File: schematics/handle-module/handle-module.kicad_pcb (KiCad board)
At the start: 4 copper layers, 80 x 42 mm, 115 parts, among them J1 2*LiFePo4@18650@1800mAh, 6,4V, J3 JST XH B3B, J4 USBASP, Q1 IRLML5203, Q10 IRLML0030, Q2 IRLML5203, Q3 IRLML0030, Q4 IRLML0030, Q5 IRLML0030, Q6 IRLML0030, Q7 IRLML0030, Q8 IRLML0030, Q9 IRLML0030, SW1 KLS7-TS3601-5.0-180, SW2 KLS7-TS3601-5.0-180, U1 STX882@443MHz, U2 SRX882@443MHz, U3 AMS1117-5.0, U4 MCP1703T-3302E, U5 ATmega328-A, U6 BQ24780S, X1 HC-49U, 8MHz

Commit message: Second board
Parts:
- moved C27 1.50 mm to (156.2, 79.7), turned to 180 degrees
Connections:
- C27 pad 2: GNDPWR -> GNDA
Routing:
- net GNDA: track 87.9 -> 99.0 mm
- net GNDPWR: track 156.4 -> 147.9 mm
- net /VBAT_BEFORE_FUSE: track 35.0 -> 33.3 mm
- net /CHARGER_SUPPLY: track 47.6 -> 47.0 mm
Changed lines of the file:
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@@
     (property "ki_keywords" "R res resistor")
     (attr smd)
-    (fp_text reference "R14" (at 0 1.65) (layer "B.SilkS")
+    (fp_text reference "R14" (at 3.1875 -0.7) (layer "B.SilkS")
         (effects (font (size 1 1) (thickness 0.15)) (justify mirror))
     )
@@
   )
   (footprint "Capacitor_SMD:C_0603_1608Metric" (layer "B.Cu")
-    (at 157.7 79.7)
+    (at 156.2 79.7 180)
     (descr "Capacitor SMD 0603 (1608 Metric), square (rectangular) end terminal, IPC_7351 nominal, (Body size source: IPC-SM-782 page 76, https://www.pcb-3d.com/wordpress/wp-content/uploads/ipc-sm-782a_amendment_1_and_2.pdf), generated with kicad-footprint-generator")
     (tags "capacitor")
@@
     (property "ki_keywords" "cap capacitor")
     (attr smd)
-    (fp_text reference "C27" (at 0 1.43) (layer "B.SilkS")
+    (fp_text reference "C27" (at 0.1 -1.5) (layer "B.SilkS")
         (effects (font (size 1 1) (thickness 0.15)) (justify mirror))
     )
@@
     (fp_line (start 0.8 0.4) (end 0.8 -0.4)
       (stroke (width 0.1) (type solid)) (layer "B.Fab"))
-    (pad "1" smd roundrect (at -0.775 0) (size 0.9 0.95) (layers "B.Cu" "B.Paste" "B.Mask") (roundrect_rratio 0.25)
+    (pad "1" smd roundrect (at -0.775 0 180) (size 0.9 0.95) (layers "B.Cu" "B.Paste" "B.Mask") (roundrect_rratio 0.25)
       (net 19 "Net-(U6-VCC)") (pintype "passive"))
-    (pad "2" smd roundrect (at 0.775 0) (size 0.9 0.95) (layers "B.Cu" "B.Paste" "B.Mask") (roundrect_rratio 0.25)
-      (net 6 "GNDPWR") (pintype "passive"))
+    (pad "2" smd roundrect (at 0.775 0 180) (size 0.9 0.95) (layers "B.Cu" "B.Paste" "B.Mask") (roundrect_rratio 0.25)
+      (net 1 "GNDA") (pintype "passive"))
     (model "${KICAD6_3DMODEL_DIR}/Capacitor_SMD.3dshapes/C_0603_1608Metric.wrl"
       (offset (xyz 0 0 0))
@@
     (effects (font (size 1.5 1.5) (thickness 0.2)) (justify left top))
   )
-  (segment (start 164.9 71.3625) (end 164.9 71.1) (width 0.2) (layer "F.Cu") (net 1))
   (segment (start 114.25 58.5) (end 113.8 58.05) (width 0.5) (layer "F.Cu") (net 1))
   (segment (start 174.55 67.05) (end 174.55 70.9375) (width 0.5) (layer "F.Cu") (net 1))
@@
   (segment (start 172.8 62.075001) (end 163 52.275001) (width 1) (layer "In1.Cu") (net 1))
   (segment (start 133.5 88.75) (end 130.5 85.75) (width 0.5) (layer "B.Cu") (net 1))
+  (segment (start 151.452449 77.8) (end 144.9 77.8) (width 0.5) (layer "B.Cu") (net 1))
   (segment (start 150.6375 88.75) (end 133.5 88.75) (width 0.5) (layer "B.Cu") (net 1))
+  (segment (start 153.352449 79.7) (end 151.452449 77.8) (width 0.5) (layer "B.Cu") (net 1))
+  (segment (start 155.425 79.7) (end 153.352449 79.7) (width 0.5) (layer "B.Cu") (net 1))
   (segment (start 151.6875 87.7) (end 150.6375 88.75) (width 0.5) (layer "B.Cu") (net 1))
   (segment (start 163.560051 78.2) (end 160.860051 80.9) (width 0.5) (layer "F.Cu") (net 2))
@@
   (segment (start 158.7 80.9) (end 158 80.2) (width 0.5) (layer "F.Cu") (net 2))
   (segment (start 131.825 56.75) (end 131.825 58.175) (width 1) (layer "F.Cu") (net 2))
-  (segment (start 157.1125 77.5125) (end 156.9 77.5125) (width 0.5) (layer "F.Cu") (net 2))
   (segment (start 115 60) (end 119.225 60) (width 0.5) (layer "F.Cu") (net 2))
   (segment (start 120.75 59.65) (end 122.975 59.65) (width 0.5) (layer "F.Cu") (net 2))
@@
   (segment (start 144.5 60.5) (end 144.355 62.9375) (width 0.5) (layer "B.Cu") (net 2))
   (segment (start 105.72 77.74) (end 106.46 77) (width 0.5) (layer "B.Cu") (net 2))
-  (segment (start 125.475 85.695) (end 125.42 85.75) (width 0.5) (layer "B.Cu") (net 2))
   (segment (start 144.355 62.9375) (end 144.48 63.0625) (width 0.5) (layer "B.Cu") (net 2))
   (segment (start 125.475 83.75) (end 125.475 85.695) (width 0.5) (layer "B.Cu") (net 2))
@@
   (segment (start 125.475 69.525) (end 127 68) (width 0.5) (layer "B.Cu") (net 4))
   (segment (start 125.5 71.7875) (end 125.5 70.05) (width 0.5) (layer "B.Cu") (net 4))
-  (segment (start 125.6125 71.9) (end 125.5 71.7875) (width 0.5) (layer "B.Cu") (net 4))
   (segment (start 125.5 70.05) (end 125.6125 69.9375) (width 0.5) (layer "B.Cu") (net 4))
   (segment (start 125.475 69.8) (end 125.475 69.525) (width 0.5) (layer "B.Cu") (net 4))
@@
   (segment (start 162.75 54.775001) (end 159.75 54.775) (width 1) (layer "B.Cu") (net 5))
   (segment (start 177 51.54) (end 173.79 54.75) (width 2) (layer "B.Cu") (net 5))
-  (segment (start 159.75 54.775) (end 157.985 54.775) (width 1) (layer "B.Cu") (net 5))
   (segment (start 173.79 54.75) (end 170 54.75) (width 2) (layer "B.Cu") (net 5))
   (segment (start 159.2 54.775) (end 154.44 54.775) (width 1) (layer "B.Cu") (net 5))
@@
   (segment (start 174.5 82.75) (end 171.525 82.75) (width 2) (layer "In1.Cu") (net 6))
   (segment (start 143.0875 83.25) (end 144.2375 82.1) (width 0.5) (layer "B.Cu") (net 6))
-  (segment (start 158.475 76.325) (end 160.45 74.35) (width 0.5) (layer "B.Cu") (net 6))
   (segment (start 176.3 61.425) (end 174.6 59.725) (width 0.2) (layer "B.Cu") (net 6))
-  (segment (start 151.625 82.1) (end 151.75 82.225) (width 0.5) (layer "B.Cu") (net 6))
   (segment (start 141.175 83.25) (end 140.225 84.2) (width 0.5) (layer "B.Cu") (net 6))
-  (segment (start 160.45 74.35) (end 162.65 74.35) (width 0.5) (layer "B.Cu") (net 6))
   (segment (start 144.2375 82.1) (end 151.625 82.1) (width 0.5) (layer "B.Cu") (net 6))
   (segment (start 169.8 68.2) (end 172.075 68.2) (width 0.2) (layer "B.Cu") (net 6))
   (segment (start 143.0875 83.25) (end 141.175 83.25) (width 0.5) (layer "B.Cu") (net 6))
   (segment (start 168.875 49) (end 173 49) (width 1) (layer "B.Cu") (net 6))
-  (segment (start 158.475 79.7) (end 158.475 76.325) (width 0.5) (layer "B.Cu") (net 6))
   (segment (start 176.3 63.975) (end 176.3 61.425) (width 0.2) (layer "B.Cu") (net 6))
   (segment (start 172.075 68.2) (end 176.3 63.975) (width 0.2) (layer "B.Cu") (net 6))
@@
   (segment (start 145.5125 74.1) (end 145.0125 74.6) (width 0.5) (layer "B.Cu") (net 7))
   (segment (start 145.725 86.3) (end 147 85.025) (width 0.5) (layer "B.Cu") (net 7))
-  (segment (start 151.7 83.825) (end 151.75 83.775) (width 0.5) (layer "B.Cu") (net 7))
   (segment (start 151.7 85.6) (end 151.7 83.825) (width 0.5) (layer "B.Cu") (net 7))
-  (segment (start 145.225 86.3) (end 145.725 86.3) (width 0.5) (layer "B.Cu") (net 7))
   (segment (start 146.775 83.25) (end 144.9125 83.25) (width 0.5) (layer "B.Cu") (net 8))
   (segment (start 147 83.475) (end 146.775 83.25) (width 0.5) (layer "B.Cu") (net 8))

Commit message: Project prepared to order
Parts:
- moved R10 0.10 mm to (152.7, 87.7)

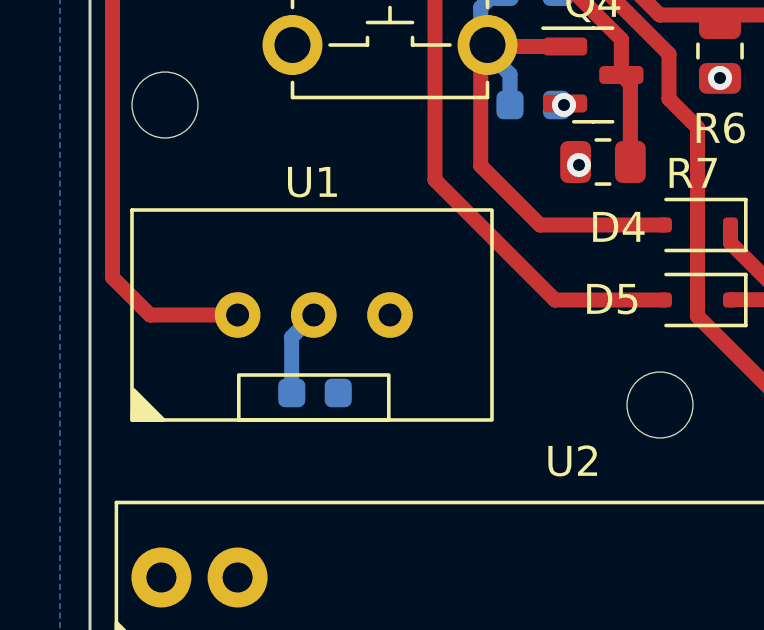
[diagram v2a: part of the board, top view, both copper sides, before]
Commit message: 1. start working under handle module; 2. rewrite stepper driver
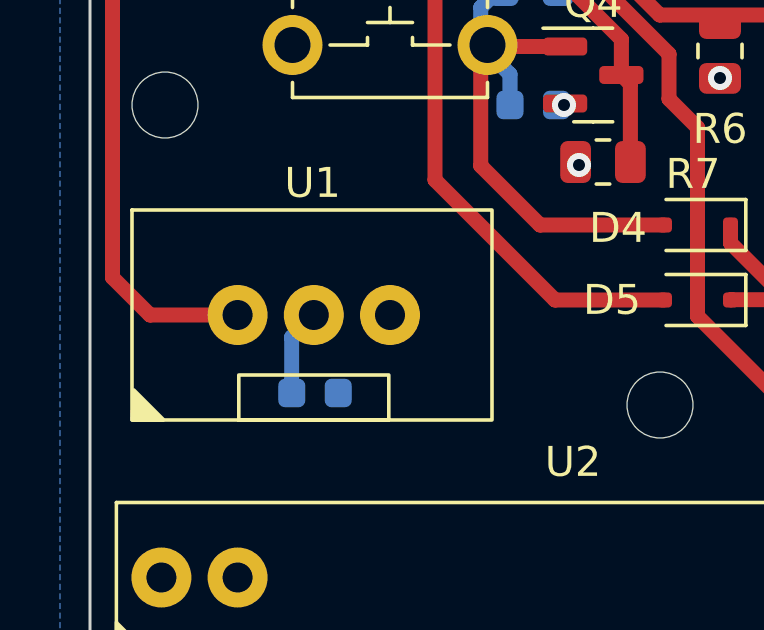
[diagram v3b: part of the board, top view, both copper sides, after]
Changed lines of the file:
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@@
     (fp_rect (start -7.06 4.5) (end 6.94 -4.5)
       (stroke (width 0.05) (type default)) (fill none) (layer "F.CrtYd"))
-    (pad "2" thru_hole circle (at -2.54 0) (size 1.524 1.524) (drill 0.762) (layers "*.Cu" "*.Mask")
+    (pad "2" thru_hole circle (at -2.54 0) (size 2 2) (drill 1) (layers "*.Cu" "*.Mask")
       (net 61 "/FM_OUT") (pinfunction "DATA") (pintype "input"))
-    (pad "3" thru_hole circle (at 0 0) (size 1.524 1.524) (drill 0.762) (layers "*.Cu" "*.Mask")
+    (pad "3" thru_hole circle (at 0 0) (size 2 2) (drill 1) (layers "*.Cu" "*.Mask")
       (net 2 "+5V") (pinfunction "VCC") (pintype "power_in"))
-    (pad "4" thru_hole circle (at 2.54 0) (size 1.524 1.524) (drill 0.762) (layers "*.Cu" "*.Mask")
+    (pad "4" thru_hole circle (at 2.54 0) (size 2 2) (drill 1) (layers "*.Cu" "*.Mask")
       (net 1 "GNDA") (pinfunction "GND") (pintype "power_in"))
   )

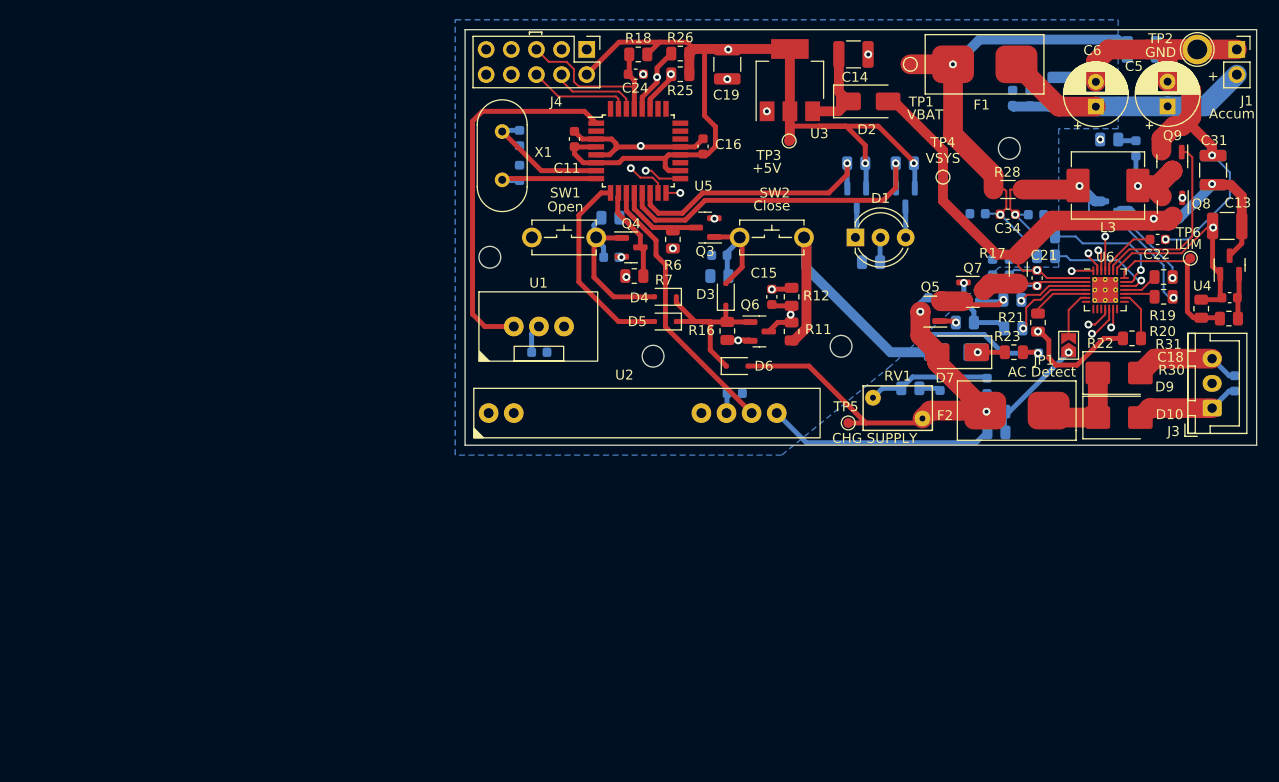
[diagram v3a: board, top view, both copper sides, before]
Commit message: 1. board: added protection against high noise in case of endstop is broken. 2. board: added step-up 7.5V -> 15V for charger. 3. firmware - added support for noise protection and some changes in stepper logic
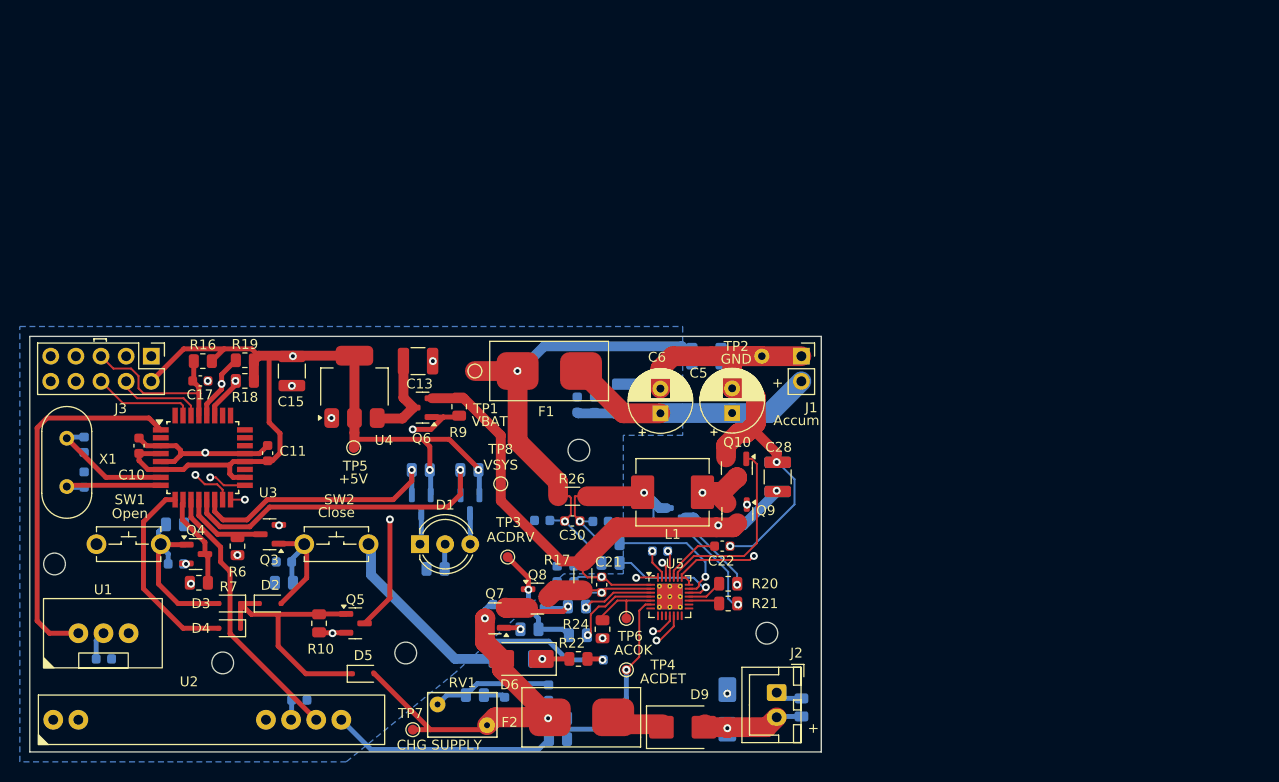
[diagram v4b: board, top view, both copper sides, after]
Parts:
- removed the C13 at (176.0, 66.8)
- removed the C15 at (130.0, 74.0)
- removed the C18 at (176.3, 74.1)
- removed the C29 at (176.8, 82.8)
- removed D10: ES2J, Diode_SMD:D_SMB
- removed the D6 at (126.5, 81.0)
- removed the J3 at (174.5, 85.2)
- removed JP1: AC Detect, Jumper:SolderJumper-2_P1.3mm_Open_TrianglePad1.0x1.5mm
- removed the R11 at (132.0, 77.5)
- removed the R12 at (132.0, 74.0)
- removed the R16 at (125.5, 77.5)
- removed the R22 at (166.4, 78.2)
- removed the R24 at (164.1, 58.1)
- removed R30: 100K, Resistor_SMD:R_0805_2012Metric
- removed R31: 7K, Resistor_SMD:R_0805_2012Metric
- removed the U4 at (176.3, 70.8)
- added D7: SMAJ26A, Diode_SMD:D_SMA, B.Cu at (125.5, 115.7)
- added H5: MountingHole, MountingHole:MountingHole_2.2mm_M2, F.Cu at (129.5, 108.0)
- added J2: Charger, Connector_JST:JST_XH_B2B-XH-A_1x02_P2.50mm_Vertical, F.Cu at (130.5, 114.0)
- added Q5: IRLML0030, Package_TO_SOT_SMD:SOT-23, F.Cu at (87.9, 107.0)
- added R10: 10K, Resistor_SMD:R_0805_2012Metric, F.Cu at (84.2, 107.0)
- added R23: 500, Resistor_SMD:R_0805_2012Metric, B.Cu at (133.0, 115.5)
- added R9: 10K, Resistor_SMD:R_0805_2012Metric, F.Cu at (98.4, 85.1)
- added TP3: ACDRV, TestPoint:TestPoint_Pad_D1.0mm, F.Cu at (103.3, 100.3)
- added TP4: ACDET, TestPoint:TestPoint_Pad_D1.0mm, F.Cu at (115.3, 111.7)
- C24: renamed from C27; value 1 uF -> 2.2 uF
- C26: renamed from C33; value 10 uF -> 4.7 uF
- C3, C4: value 10 nF -> 100 nF
- C8: value 1 uF -> 2.2 uF
- D2: value 15MQ030NPBF -> BAT760; footprint Diode_SMD:D_SMA -> Diode_SMD:D_SOD-323F
- D3, D4, D5: value BAV21WS -> BAT760
- Q6: value IRLML0030 -> IRLML5203
- R13: value 4R7 -> 5
- R14, R15: value 4K -> 3K9
- R20: renamed from R19; value 4K -> 3K3
- R5: value 1K -> 620
- R8: value 2R -> 5R
- TP2: footprint TestPoint:TestPoint_Plated_Hole_D2.0mm -> Library:TestPoint_Plated_Hole_D1.0mm
- TP6: value ILIM -> ACOK
- moved D2 78.9 mm to (79.3, 105.0)
- moved TP6 67.6 mm to (115.3, 106.5), turned to 0 degrees
- moved C25 63.0 mm to (118.7, 99.7), turned to 180 degrees
- moved D3 59.1 mm to (75.2, 105.0), turned to 180 degrees
- moved D9 56.8 mm to (121.0, 117.5)
- moved D4 55.3 mm to (75.2, 107.5)
- moved TP8 54.4 mm to (102.6, 92.9)
- moved C26 54.1 mm to (107.4, 114.0)
- moved R11 54.1 mm to (108.4, 116.6)
- moved R12 54.1 mm to (108.4, 118.7)
- moved Q2 53.8 mm to (94.6, 95.0)
- moved C14 53.8 mm to (102.6, 105.1)
- moved C16 53.8 mm to (106.2, 105.5)
- moved C3 53.8 mm to (69.8, 101.0)
- moved C31 53.8 mm to (106.8, 96.6)
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- renumbered C11 to C10, C16 to C11, C10 to C12, C14 to C13, C12 to C14, C19 to C15, C17 to C16, C24 to C17, C25 to C18, C26 to C19, C28 to C25, C30 to C27, C31 to C28, C32 to C29, C34 to C30, C35 to C31, C36 to C32, D7 to D6, J4 to J3, L3 to L1, Q9 to Q10, Q10 to Q11, Q5 to Q7, Q7 to Q8, Q8 to Q9, R9 to R11, R10 to R12, R18 to R16, R25 to R18, R26 to R19, R20 to R21, R23 to R22, R21 to R24, R27 to R25, R28 to R26, R29 to R27, TP3 to TP5, TP5 to TP7, TP4 to TP8, U5 to U3, U3 to U4, U6 to U5
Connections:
- net /CHARGER_PHASE renamed Net-(Q10-D)
- C13 pad 1: Net-(D2-K) -> Net-(Q6-D)
- C25 pad 1: Net-(C28-Pad1) -> Net-(U5-BTST)
- D2 pad 2: /VSYS -> /CLOSE_BUTTON
- D3 pad 1: Net-(D3-K) -> Net-(D2-K)
- D3 pad 2: /CLOSE_BUTTON -> /OPEN_BUTTON
- D4 pad 1: Net-(D3-K) -> Net-(D2-K)
- D4 pad 2: /OPEN_BUTTON -> /IC_POWER_UP
- D5 pad 1: Net-(D3-K) -> Net-(D2-K)
- D5 pad 2: /POWER_UP_IC -> /CHARGER_SUPPLY
- Q6 pad 1: Net-(D3-K) -> Net-(Q5-D)
- Q6 pad 2: GNDA -> /VSYS
- R11 pad 2: Net-(JP1-A) -> Net-(U5-ACDET)
- R12 pad 1: Net-(JP1-A) -> Net-(U5-ACDET)
- R24 pad 1: Net-(U6-ACOK) -> Net-(U5-ACOK)
- TP6 pad 1: /CHARGER_ILIM -> Net-(U5-ACOK)
- U3 pad 9: /POWER_UP_IC -> /IC_POWER_UP
- U4 pad 3: Net-(D2-K) -> Net-(Q6-D)
- U5 pad 13: Net-(Q6-D) -> unconnected-(U5-CMPIN-Pad13)
- U5 pad 16: Net-(U6-TB_STAT#) -> unconnected-(U5-TB_STAT#-Pad16)
- U5 pad 21: /CHARGER_ILIM -> GNDA
- U5 pad 25: /CHARGER_BOOST -> Net-(U5-BTST)
- U5 pad 5: Net-(U6-ACOK) -> Net-(U5-ACOK)
- U5 pad 6: Net-(JP1-B) -> Net-(U5-ACDET)
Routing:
- net Net-(Q6-D): track 46.4 -> 9.17 mm, vias 2 -> 0
- net Net-(Q5-D): track 0.00 -> 27.9 mm, vias 0 -> 2
- net Net-(U5-ACDET): track 0.00 -> 20.2 mm, vias 0 -> 1
- net /POWER_UP_IC: track 20.2 -> 0.00 mm
- net /IC_POWER_UP: track 0.00 -> 20.2 mm
- net Net-(D3-K): track 18.2 -> 0.00 mm
- net Net-(D2-K): track 9.19 -> 27.3 mm
- net /CHARGER_ILIM: track 16.8 -> 0.00 mm
- net +5V: track 216.3 -> 201.6 mm
- net /CHARGER_BOOST: track 13.5 -> 0.00 mm, vias 2 -> 0
- net /VBAT: track 136.8 -> 125.6 mm
- net GNDA: track 99.0 -> 87.8 mm, vias 10 -> 9
- net Net-(JP1-A): track 10.9 -> 0.00 mm, vias 1 -> 0
- net Net-(D10-A): track 10.6 -> 0.00 mm
- net Net-(U5-ACOK): track 0.00 -> 7.54 mm
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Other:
- board text added: "ACW-handle-v1.1"
- board text removed: "ACW-handle-v1.0"

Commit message: another iteration for outdorr and handle modules
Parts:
- removed TP1: VBAT, TestPoint:TestPoint_Pad_D1.0mm
- added C33: 100 nF, Capacitor_SMD:C_0603_1608Metric, B.Cu at (107.2, 94.2)
- added JP1: PROCHOT#_EN, Jumper:SolderJumper-2_P1.3mm_Open_TrianglePad1.0x1.5mm, F.Cu at (116.5, 111.6)
- added NT2: NetTie_2, NetTie:NetTie-2_SMD_Pad0.5mm, F.Cu at (110.6, 98.2)
- added NT3: NetTie_2, NetTie:NetTie-2_SMD_Pad0.5mm, F.Cu at (109.2, 98.2)
- added R28: 10, Resistor_SMD:R_0805_2012Metric, B.Cu at (106.6, 100.4)
- added R29: 10, Resistor_SMD:R_0805_2012Metric, B.Cu at (106.6, 98.4)
- added U7: INA219, Package_SO:SOIC-8_3.9x4.9mm_P1.27mm, B.Cu at (104.4, 89.6)
- R23: value 500 -> 2K2
- R5: moved to F.Cu
- moved D7 21.1 mm to (104.4, 116.0)
- moved TP2 18.4 mm to (114.0, 90.6)
- moved F1 16.5 mm to (124.0, 81.4)
- moved C7 16.0 mm to (99.6, 80.8), turned to -90 degrees
- moved C5 12.9 mm to (114.2, 80.6), turned to -90 degrees
- moved C6 12.6 mm to (107.2, 80.7), turned to -90 degrees
- moved C8 10.5 mm to (102.7, 80.2), turned to -90 degrees
- moved C9 7.52 mm to (104.5, 80.2), turned to 90 degrees
- moved R5 7.37 mm to (98.0, 94.4)
- moved NT1 5.80 mm to (121.8, 85.8)
- moved C12 5.00 mm to (98.0, 115.6), turned to 0 degrees
- moved RV1 4.09 mm to (97.2, 117.7), turned to 90 degrees
- moved C32 3.22 mm to (120.6, 81.6), turned to -90 degrees
- moved TP4 2.82 mm to (112.6, 112.5)
- moved J1 2.60 mm to (133.0, 82.6), turned to 180 degrees
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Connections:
- net Net-(Q5-D) renamed /PROCHOT#
- C22 pad 1: Net-(U5-REGN) -> Net-(U5-ILIM)
- C5 pad 1: /VBAT_BEFORE_FUSE -> /VBAT
- C6 pad 1: /VBAT_BEFORE_FUSE -> /VBAT
- C7 pad 1: /VBAT_BEFORE_FUSE -> /VBAT
- C8 pad 1: /VBAT_BEFORE_FUSE -> /VBAT
- C9 pad 2: /VBAT_BEFORE_FUSE -> /VBAT
- D7 pad 1: Net-(D7-A1) -> /CHARGER_SUPPLY
- D9 pad 2: Net-(D7-A1) -> Net-(D9-A)
- F1 pad 1: /VBAT_BEFORE_FUSE -> Net-(J1-Pin_2)
- J1 pad 2: /VBAT_BEFORE_FUSE -> Net-(J1-Pin_2)
- J2 pad 2: Net-(D7-A1) -> Net-(D9-A)
- R23 pad 1: Net-(D7-A1) -> Net-(D9-A)
- R25 pad 1: /CHARGER_SRP -> Net-(U5-SRP)
- R25 pad 2: /CHARGER_BATSRC -> /CHARGER_SRP
- R27 pad 1: /VBAT -> /CHARGER_SRN
- R27 pad 2: /CHARGER_SRN -> Net-(U5-SRN)
- TP2 pad 1: GNDPWR -> GNDA
- U5 pad 10: unconnected-(U5-PROCHOT#-Pad10) -> Net-(JP1-A)
- U5 pad 13: unconnected-(U5-CMPIN-Pad13) -> GNDPWR
- U5 pad 19: /CHARGER_SRN -> Net-(U5-SRN)
- U5 pad 20: /CHARGER_SRP -> Net-(U5-SRP)
- U5 pad 21: GNDA -> Net-(U5-ILIM)
- U5 pad 24: Net-(U5-REGN) -> Net-(U5-ILIM)
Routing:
- net /SCL: track 65.6 -> 101.8 mm, vias 2 -> 3
- net /SDA: track 60.7 -> 95.2 mm, vias 2 -> 3
- net /VBAT_BEFORE_FUSE: track 33.3 -> 0.00 mm
- net /PROCHOT#: track 27.9 -> 57.3 mm, vias 2 -> 4
- net GNDA: track 87.8 -> 104.0 mm, vias 9 -> 10
- net +5V: track 201.6 -> 216.1 mm, vias 6 -> 8
- net Net-(U5-SRP): track 0.00 -> 13.3 mm, vias 0 -> 1
- net Net-(U5-SRN): track 0.00 -> 11.7 mm, vias 0 -> 1
- net Net-(U5-ILIM): track 0.00 -> 11.1 mm, vias 0 -> 2
- net Net-(U7-VIN_+): track 0.00 -> 10.6 mm
- net Net-(D7-A1): track 10.3 -> 0.00 mm, vias 1 -> 0
- net Net-(D9-A): track 0.00 -> 8.37 mm
- net Net-(U7-VIN_-): track 0.00 -> 7.88 mm
- net /CHARGER_SRP: track 13.3 -> 6.02 mm
- net Net-(J1-Pin_2): track 0.00 -> 6.31 mm
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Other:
- board text added: "ACW-handle-v1.2"
- board text removed: "ACW-handle-v1.1"
